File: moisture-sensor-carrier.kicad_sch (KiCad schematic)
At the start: 60 parts, among them J1 USB-C receptacle, J2 Battery - Adafruit 1578, J3 Solar panel, J4 SWD 10p 1.27mm, J5 U.FL-R-SMT-1(10) antenna, U1 nRF54L15-QFAA, U2 nPM1300-QEAA, U3 FDC1004, U4 SHT45-AD1F, U5 TPS7A1650 5V LDO, X1 CM8V-T1A 32.768kHz CL=7pF 20p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, X2 FA-128 32MHz CL=8pF

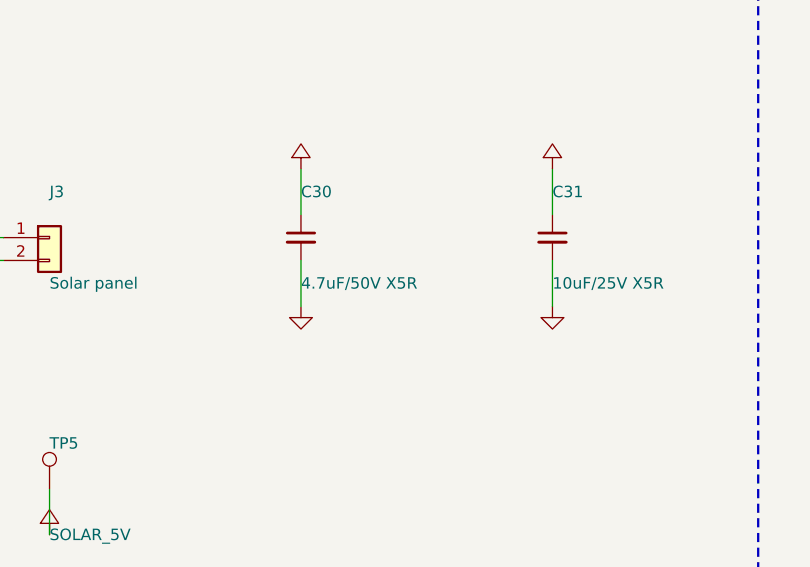
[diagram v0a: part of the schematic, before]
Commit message: Consolidate moisture sensor PCB design and BOM
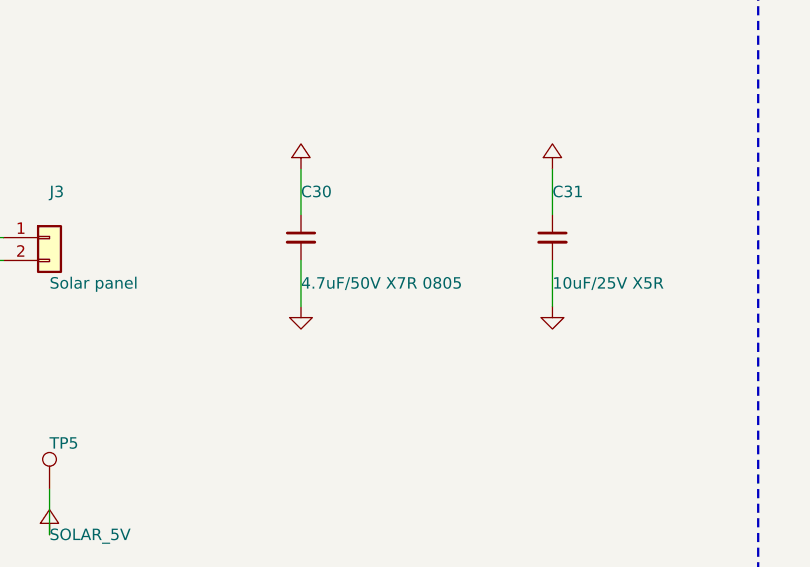
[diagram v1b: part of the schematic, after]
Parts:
- C11: MPN (none) -> GRM0335C1ER30BA01D
- C30: value 4.7uF/50V X5R -> 4.7uF/50V X7R 0805; footprint Capacitor_SMD:C_0603_1608Metric_Pad1.08x0.95mm_HandSolder -> Capacitor_SMD:C_0805_2012Metric_Pad1.18x1.45mm_HandSolder; MPN (none) -> GRM21BR61H475KA12L
- C31: MPN (none) -> CL10A106MA8NRNC
- D3: MPN (none) -> LTST-C190KGKT
- D4: MPN (none) -> LTST-C190KRKT
- D5: MPN (none) -> RB751V-40_R1_00001
- FB1: MPN (none) -> MMZ1005S121CT000
- J1: MPN (none) -> TYPE-C-31-M-12
- TH1: footprint Resistor_SMD:R_0603_1608Metric_Pad0.98x0.95mm_HandSolder -> footprints:Thermistor_SEMITEC_103JT_Wired; MPN (none) -> 103JT-025
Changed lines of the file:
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@@
 			(effects (font (size 1.27 1.27)) (hide yes))
 		)
+		(property "MPN" "TYPE-C-31-M-12"
+			(at 33.02 381.0 0)
+			(effects (font (size 1.27 1.27)) (hide yes))
+		)
 		(pin "A1")
 		(pin "A2")
@@
 			(effects (font (size 1.27 1.27)) (hide yes))
 		)
+		(property "MPN" "RB751V-40_R1_00001"
+			(at 60.96 441.96 0)
+			(effects (font (size 1.27 1.27)) (hide yes))
+		)
 		(pin "1")
 		(pin "2")
@@
 			(effects (font (size 1.27 1.27)) (justify left))
 		)
-		(property "Value" "4.7uF/50V X5R"
+		(property "Value" "4.7uF/50V X7R 0805"
 			(at 116.84 447.04 0)
 			(effects (font (size 1.27 1.27)) (justify left))
 		)
-		(property "Footprint" "Capacitor_SMD:C_0603_1608Metric_Pad1.08x0.95mm_HandSolder"
+		(property "Footprint" "Capacitor_SMD:C_0805_2012Metric_Pad1.18x1.45mm_HandSolder"
+			(at 116.84 441.96 0)
+			(effects (font (size 1.27 1.27)) (hide yes))
+		)
+		(property "MPN" "GRM21BR61H475KA12L"
 			(at 116.84 441.96 0)
 			(effects (font (size 1.27 1.27)) (hide yes))
@@
 			(effects (font (size 1.27 1.27)) (hide yes))
 		)
+		(property "MPN" "CL10A106MA8NRNC"
+			(at 144.78 441.96 0)
+			(effects (font (size 1.27 1.27)) (hide yes))
+		)
 		(pin "1")
 		(pin "2")
@@
 			(effects (font (size 1.27 1.27)) (hide yes))
 		)
+		(property "MPN" "MMZ1005S121CT000"
+			(at 637.54 50.8 0)
+			(effects (font (size 1.27 1.27)) (hide yes))
+		)
 		(pin "1")
 		(pin "2")
@@
 			(effects (font (size 1.27 1.27)) (justify left))
 		)
-		(property "Footprint" "Resistor_SMD:R_0603_1608Metric_Pad0.98x0.95mm_HandSolder"
+		(property "Footprint" "footprints:Thermistor_SEMITEC_103JT_Wired"
+			(at 342.9 373.38 0)
+			(effects (font (size 1.27 1.27)) (hide yes))
+		)
+		(property "MPN" "103JT-025"
 			(at 342.9 373.38 0)
 			(effects (font (size 1.27 1.27)) (hide yes))
@@
 			(effects (font (size 1.27 1.27)) (hide yes))
 		)
+		(property "MPN" "LTST-C190KGKT"
+			(at 314.96 401.32 0)
+			(effects (font (size 1.27 1.27)) (hide yes))
+		)
 		(pin "1")
 		(pin "2")
@@
 			(effects (font (size 1.27 1.27)) (hide yes))
 		)
+		(property "MPN" "LTST-C190KRKT"
+			(at 370.84 401.32 0)
+			(effects (font (size 1.27 1.27)) (hide yes))
+		)
 		(pin "1")
 		(pin "2")
@@
 			(at 104.14 60.96 0)
 			(effects (font (size 1.27 1.27)) (hide yes))
+		)
+		(property "MPN" "GRM0335C1ER30BA01D"
+			(at 104.14 60.96 0)
+			(effects (font (size 1.27 1.27)) (hide yes))
